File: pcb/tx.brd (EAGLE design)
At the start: 28 x 36.5 mm, 55 parts, among them Q1 BSS84, U3 MCP73831T-2ACI/OT, Y1 CRYSTAL-26MHZSMD-3.2X2.5

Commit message: before trail run
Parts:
- C8, C9: value 22pF -> 12pF
- Y1: value CRYSTAL-26MHZSMD-3.2X2.5 -> 16MHz_12pF
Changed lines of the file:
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@@
 <attribute name="NAME" x="18.2372" y="24.1681" size="0.8128" layer="25"/>
 </element>
-<element name="C8" library="clock" package="0805" value="22pF" x="20.0152" y="19.812" smashed="yes" rot="R90">
+<element name="C8" library="clock" package="0805" value="12pF" x="20.0152" y="19.812" smashed="yes" rot="R90">
 <attribute name="NAME" x="20.4089" y="17.1196" size="0.8128" layer="25" rot="R90"/>
 </element>
-<element name="C9" library="clock" package="0805" value="22pF" x="17.4498" y="23.0886" smashed="yes">
+<element name="C9" library="clock" package="0805" value="12pF" x="17.4498" y="23.0886" smashed="yes">
 <attribute name="NAME" x="16.0655" y="22.225" size="0.8128" layer="25" rot="R90"/>
 </element>
-<element name="Y1" library="SparkFun-Clocks" package="CRYSTAL-SMD-3.2X2.5MM" value="CRYSTAL-26MHZSMD-3.2X2.5" x="17.399" y="20.0914" smashed="yes" rot="R90">
+<element name="Y1" library="SparkFun-Clocks" package="CRYSTAL-SMD-3.2X2.5MM" value="16MHz_12pF" x="17.399" y="20.0914" smashed="yes" rot="R90">
 <attribute name="PROD_ID" value="XTAL-12454" x="44.704" y="-0.4826" size="1.778" layer="27" rot="R90" display="off"/>
 </element>

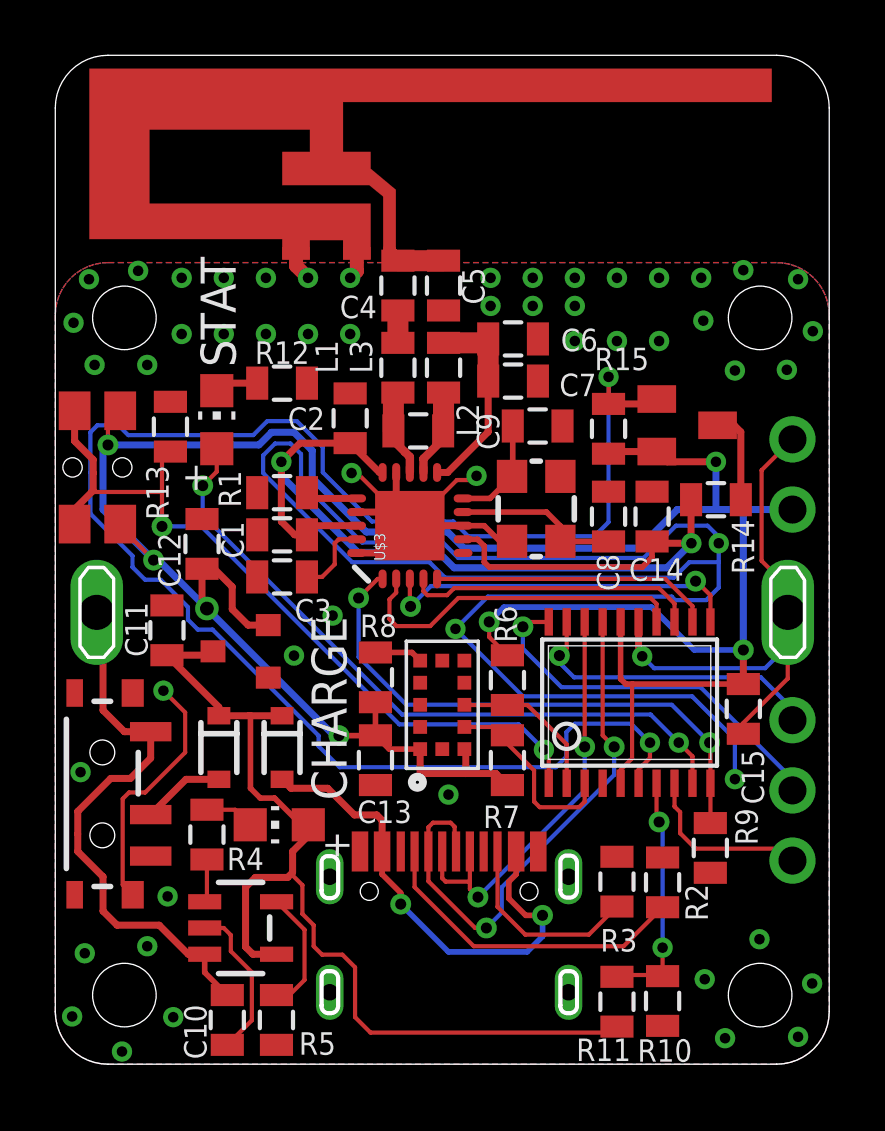
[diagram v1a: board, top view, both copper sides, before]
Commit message: centered usbc footprint, adjusted board layout
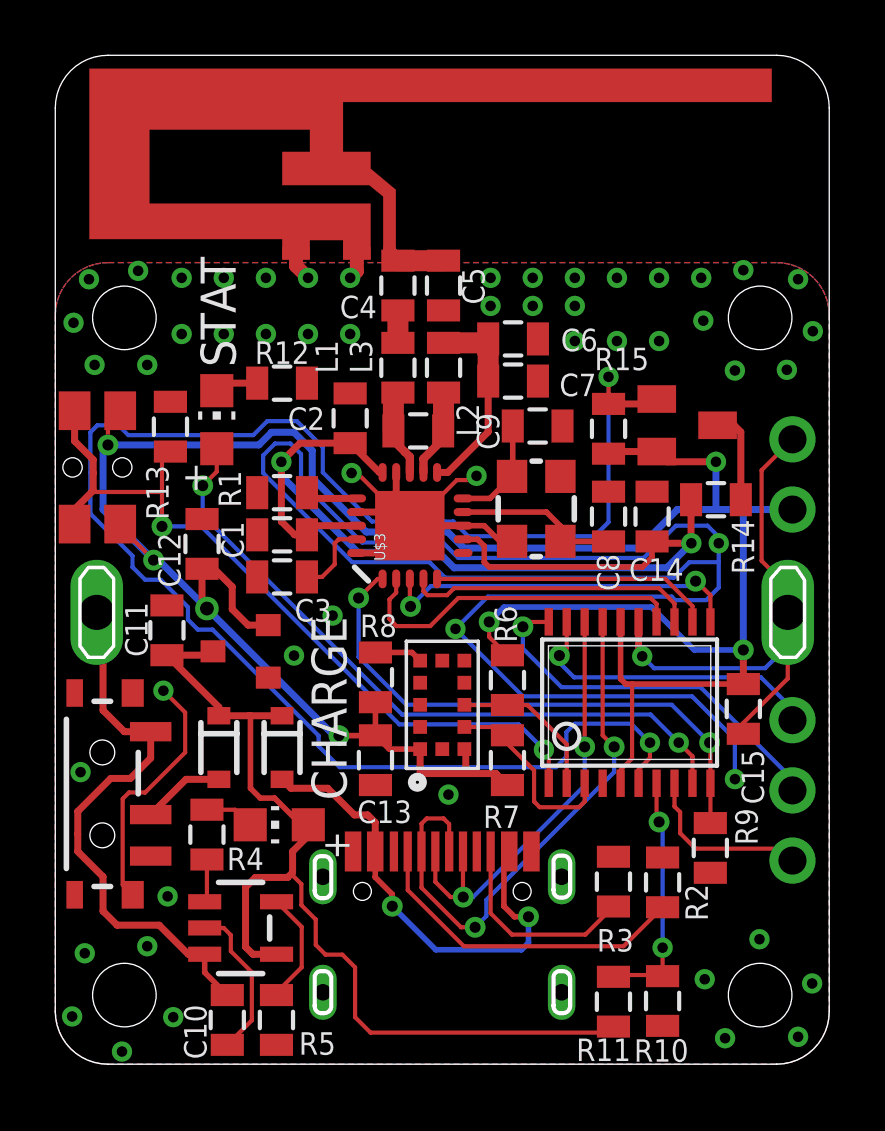
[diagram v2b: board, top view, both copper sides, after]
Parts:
- removed U$4: USBC_16P, my_usbc_16p:USBC_16P_FOOT
- added U$5: USBC_16P_CENTERED, my_usbc_16p_centered:USBC_16P_FOOT
- moved R10 0.13 mm to (20.2, 2.26)
- moved R3 0.13 mm to (20.2, 6.60)
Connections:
- net GND: now also U$5.A1B12, U$5.B11A12, U$5.P$13, U$5.P$14, U$5.P$15, U$5.P$16; no longer U$4.A1B12, U$4.B11A12, U$4.P$13, U$4.P$14, U$4.P$15, U$4.P$16
- net N$10: now also U$5.B5; no longer U$4.B5
- net N$11: now also U$5.A5; no longer U$4.A5
- net N$18: now also U$5.A6, U$5.B6; no longer U$4.A6, U$4.B6
- net N$26: now also U$5.A4B9, U$5.B4A9; no longer U$4.A4B9, U$4.B4A9
- net N$34: now also U$5.A7, U$5.B7; no longer U$4.A7, U$4.B7
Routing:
- net N$26: track 17.7 -> 17.0 mm
- net N$18: track 15.3 -> 16.0 mm
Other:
- board text added: "PD1 190523"
- board text removed: "REV4 MAR2 19"

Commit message: foodprint adjustment, coord file
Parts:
- renumbered S2 to SW1, U$10 to SW2, U$2 to IC1, U$3 to IC2, U$5 to U2, U$9 to U4

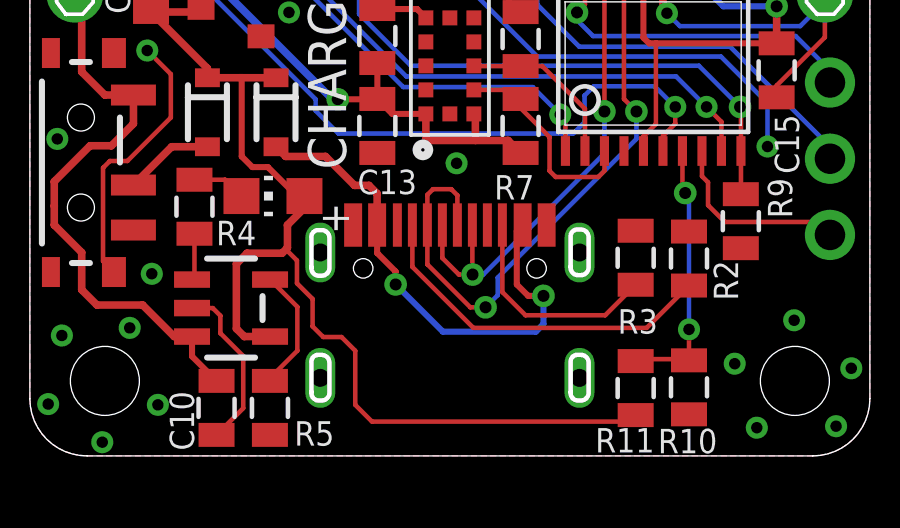
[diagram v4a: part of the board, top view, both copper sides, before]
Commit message: updated USBC connector, check_battery DBZ
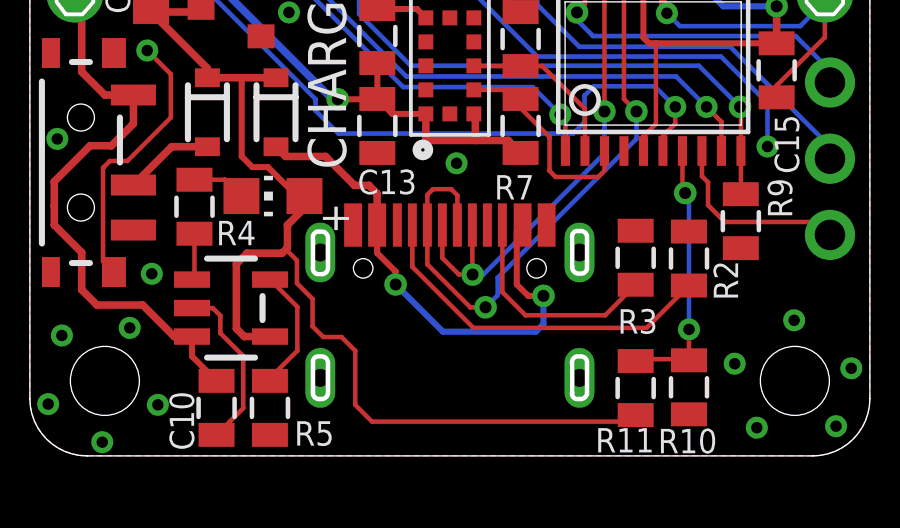
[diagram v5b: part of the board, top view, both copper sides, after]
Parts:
- U2: value USBC_16P_CENTERED -> USBC_16P; device my_usbc_16p_centered:USBC_16P_FOOT -> my_usbc_16p:USBC_16P_FOOT
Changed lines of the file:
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@@
 <grid distance="10" unitdist="mil" unit="mil" style="lines" multiple="1" display="no" altdistance="1" altunitdist="mil" altunit="mil"/>
 <layers>
-<layer number="1" name="Top" color="4" fill="1" visible="no" active="yes"/>
+<layer number="1" name="Top" color="4" fill="1" visible="yes" active="yes"/>
 <layer number="2" name="Route2" color="16" fill="1" visible="no" active="no"/>
 <layer number="3" name="Route3" color="17" fill="1" visible="no" active="no"/>
@@
 <layer number="19" name="Unrouted" color="6" fill="1" visible="yes" active="yes"/>
 <layer number="20" name="Dimension" color="24" fill="1" visible="yes" active="yes"/>
-<layer number="21" name="tPlace" color="7" fill="1" visible="no" active="yes"/>
+<layer number="21" name="tPlace" color="7" fill="1" visible="yes" active="yes"/>
 <layer number="22" name="bPlace" color="7" fill="1" visible="yes" active="yes"/>
-<layer number="23" name="tOrigins" color="15" fill="1" visible="no" active="yes"/>
+<layer number="23" name="tOrigins" color="15" fill="1" visible="yes" active="yes"/>
 <layer number="24" name="bOrigins" color="15" fill="1" visible="yes" active="yes"/>
-<layer number="25" name="tNames" color="7" fill="1" visible="no" active="yes"/>
+<layer number="25" name="tNames" color="7" fill="1" visible="yes" active="yes"/>
 <layer number="26" name="bNames" color="7" fill="1" visible="yes" active="yes"/>
 <layer number="27" name="tValues" color="7" fill="1" visible="no" active="yes"/>
@@
 <layer number="37" name="tTest" color="7" fill="1" visible="no" active="yes"/>
 <layer number="38" name="bTest" color="7" fill="1" visible="no" active="yes"/>
-<layer number="39" name="tKeepout" color="4" fill="11" visible="no" active="yes"/>
+<layer number="39" name="tKeepout" color="4" fill="11" visible="yes" active="yes"/>
 <layer number="40" name="bKeepout" color="1" fill="11" visible="yes" active="yes"/>
-<layer number="41" name="tRestrict" color="4" fill="10" visible="no" active="yes"/>
+<layer number="41" name="tRestrict" color="4" fill="10" visible="yes" active="yes"/>
 <layer number="42" name="bRestrict" color="1" fill="10" visible="yes" active="yes"/>
 <layer number="43" name="vRestrict" color="2" fill="10" visible="no" active="yes"/>
 <layer number="44" name="Drills" color="7" fill="1" visible="no" active="yes"/>
 <layer number="45" name="Holes" color="7" fill="1" visible="no" active="yes"/>
-<layer number="46" name="Milling" color="3" fill="1" visible="no" active="yes"/>
+<layer number="46" name="Milling" color="3" fill="1" visible="yes" active="yes"/>
 <layer number="47" name="Measures" color="7" fill="1" visible="no" active="yes"/>
 <layer number="48" name="Document" color="7" fill="1" visible="no" active="yes"/>
 <layer number="49" name="Reference" color="7" fill="1" visible="no" active="yes"/>
 <layer number="50" name="dxf" color="7" fill="1" visible="no" active="no"/>
-<layer number="51" name="tDocu" color="7" fill="1" visible="no" active="yes"/>
+<layer number="51" name="tDocu" color="7" fill="1" visible="yes" active="yes"/>
 <layer number="52" name="bDocu" color="7" fill="1" visible="yes" active="yes"/>
 <layer number="53" name="tGND_GNDA" color="7" fill="1" visible="no" active="no"/>
@@
 <attribute name="VALUE" x="21.4122" y="21.971" size="0.4064" layer="27" rot="R90"/>
 </element>
-<element name="U2" library="my_usbc_16p_centered" package="USBC_16P_FOOT" value="USBC_16P_CENTERED" x="14" y="3.8481"/>
+<element name="U2" library="my_usbc_16p" package="USBC_16P_FOOT" value="USBC_16P" x="14" y="3.8481"/>
 </elements>
 <signals>

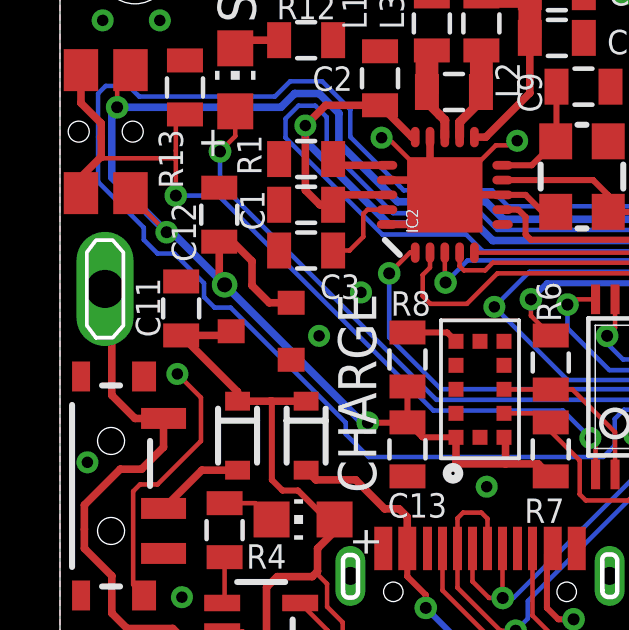
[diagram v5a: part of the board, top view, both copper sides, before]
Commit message: added more clearance near battery terminal
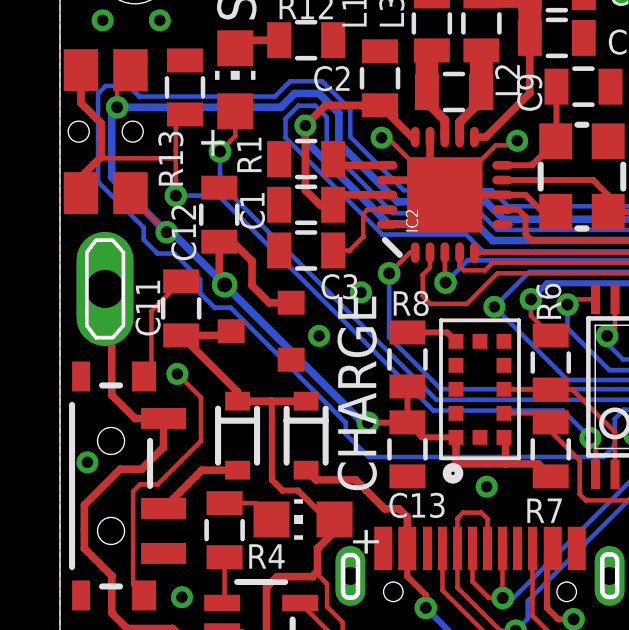
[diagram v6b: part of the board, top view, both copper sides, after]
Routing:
- net GND: track 116.2 -> 119.9 mm
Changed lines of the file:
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@@
 <setting verticaltext="up"/>
 </settings>
-<grid distance="10" unitdist="mil" unit="mil" style="lines" multiple="1" display="no" altdistance="1" altunitdist="mil" altunit="mil"/>
+<grid distance="1" unitdist="mil" unit="mil" style="lines" multiple="1" display="no" altdistance="1" altunitdist="mil" altunit="mil"/>
 <layers>
 <layer number="1" name="Top" color="4" fill="1" visible="yes" active="yes"/>
@@
 <circle x="2.5" y="2.5" radius="2.25" width="0" layer="30"/>
 <circle x="25.5" y="2.5" radius="2.25" width="0" layer="30"/>
+<polygon width="0.1524" layer="41">
+<vertex x="0.8382" y="18.5928"/>
+<vertex x="2.2098" y="18.5928"/>
+<vertex x="2.794" y="18.0086"/>
+<vertex x="2.794" y="14.4272"/>
+<vertex x="2.5146" y="14.1478"/>
+<vertex x="0.5588" y="14.1478"/>
+<vertex x="0.3556" y="14.351"/>
+<vertex x="0.3556" y="18.1356"/>
+<vertex x="0.8128" y="18.5928"/>
+</polygon>
 </plain>
 <attributes>
@@
 <contactref element="U2" pad="P$13"/>
 <contactref element="U2" pad="A1B12"/>
+<wire x1="4.0386" y1="16.5972" x2="3.048" y2="15.6066" width="0.1524" layer="1"/>
+<wire x1="3.048" y1="13.6752" x2="2.8018" y2="13.429" width="0.1524" layer="1"/>
+<wire x1="3.048" y1="15.6066" x2="3.048" y2="13.6752" width="0.1524" layer="1"/>
 </signal>
 <signal name="+3V3">
@@
 <wire x1="9.525" y1="11.5062" x2="9.525" y2="11.8872" width="0.1524" layer="16"/>
 <wire x1="9.525" y1="11.8872" x2="5.6896" y2="15.7226" width="0.1524" layer="16"/>
-<wire x1="5.1562" y1="15.7226" x2="4.8006" y2="16.0782" width="0.1524" layer="16"/>
-<wire x1="4.8006" y1="16.0782" x2="4.8006" y2="16.5354" width="0.1524" layer="16"/>
-<wire x1="4.8006" y1="16.5354" x2="3.81" y2="17.526" width="0.1524" layer="16"/>
+<wire x1="5.1562" y1="15.7226" x2="4.6736" y2="16.2052" width="0.1524" layer="16"/>
+<wire x1="4.6736" y1="16.2052" x2="4.6736" y2="16.6624" width="0.1524" layer="16"/>
+<wire x1="4.6736" y1="16.6624" x2="3.81" y2="17.526" width="0.1524" layer="16"/>
 <wire x1="3.81" y1="17.526" x2="3.2512" y2="17.526" width="0.1524" layer="16"/>
 <wire x1="3.2512" y1="17.526" x2="2.794" y2="17.9832" width="0.1524" layer="16"/>
